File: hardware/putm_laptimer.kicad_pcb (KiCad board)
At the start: 4 copper layers, 83 x 63.5 mm, 54 parts, among them J1 Conn_01x22, J2 Conn_01x22, J3 Conn_01x22, J4 Conn_01x22, J5 2092-1372, J6 2092-1372, J7 Conn_02x05_Odd_Even, J8 Conn_01x09, SW1 SW_Push, SW2 SW_Push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

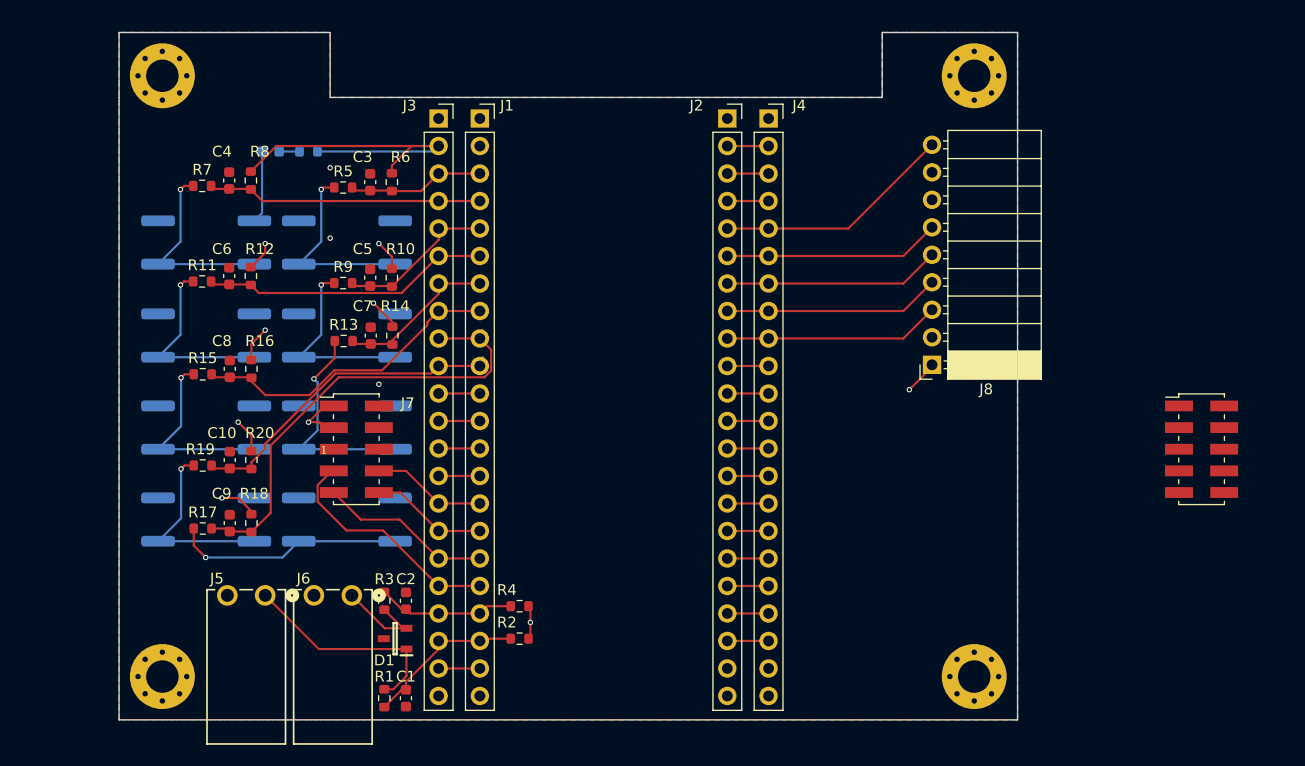
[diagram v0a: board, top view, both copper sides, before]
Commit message: deleted buttons on board and added hawrin connector
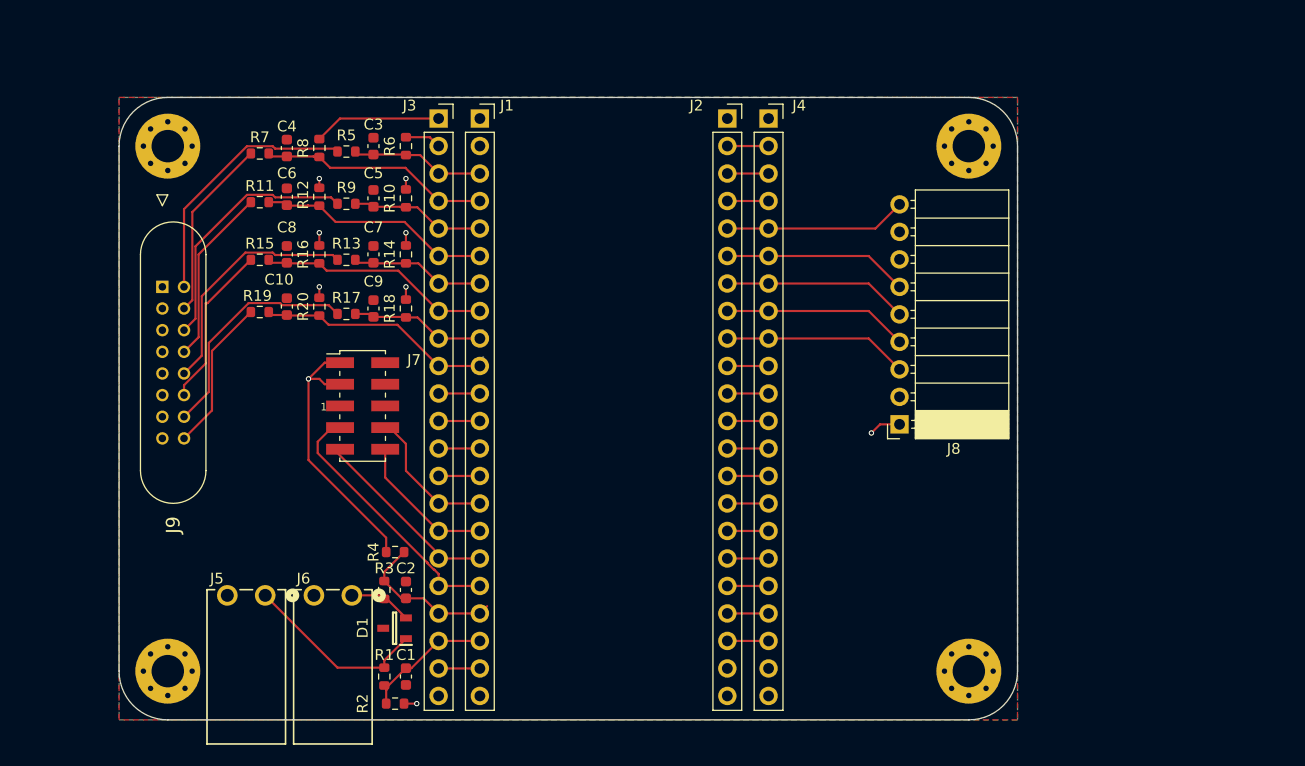
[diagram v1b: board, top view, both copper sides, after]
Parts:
- removed D2: Red, LED_SMD:LED_0603_1608Metric
- removed the J7 at (216.0, 91.5)
- removed R21: 330R, Resistor_SMD:R_0603_1608Metric
- removed SW1, SW2, SW3, SW4, SW5, SW6, SW7, SW8: SW_Push, Button_Switch_SMD:SW_Push_1P1T_NO_CK_KSC6xxG
- added J9: M80-5001605, Footprint:M80-50016YY_2, F.Cu at (120.0, 76.5)
- J5, J6: value 2092-1372 -> 2091-1372
- moved R18 24.4 mm to (142.5, 78.5)
- moved C9 23.9 mm to (139.5, 78.5)
- moved R17 23.9 mm to (137.0, 79.0)
- moved R20 15.5 mm to (134.5, 78.3)
- moved C10 15.1 mm to (131.5, 78.3)
- moved R19 15.1 mm to (129.0, 78.8)
- moved R2 13.0 mm to (141.5, 115.0)
- moved R4 12.5 mm to (141.5, 101.0), turned to 180 degrees
- moved R16 12.3 mm to (134.5, 73.5)
- moved C8 11.8 mm to (131.5, 73.5)
- moved R15 11.8 mm to (129.0, 74.0)
- moved R12 9.68 mm to (134.5, 68.2)
- moved C6 9.06 mm to (131.5, 68.2)
- moved R11 9.06 mm to (129.0, 68.7)
- moved R14 7.60 mm to (142.5, 73.5)
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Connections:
- net /IO15_DRIVER_BTN renamed /IO15_PIN
- net /IO16_ADD1_BTN renamed /IO16_PIN
- net /IO17_ADD2_BTN renamed /IO17_PIN
- net /IO4_STOP_BTN renamed /IO4_PIN
- net /IO5_WIFI_BTN renamed /IO5_PIN
- net /IO6_DOO_BTN renamed /IO6_PIN
- net /IO7_OC_BTN renamed /IO7_PIN
- C3 pad 1: /RST_BTN -> /RST_PIN
- J1 pad 3: /RST_BTN -> /RST_PIN
- J3 pad 3: /RST_BTN -> /RST_PIN
- R11 pad 2: Net-(R11-Pad2) -> /DOO_BTN
- R13 pad 2: Net-(R13-Pad2) -> /OC_BTN
- R15 pad 2: Net-(R15-Pad2) -> /DRIVER_BTN
- R17 pad 2: Net-(R17-Pad2) -> /ADD1_BTN
- R19 pad 2: Net-(R19-Pad2) -> /ADD2_BTN
- R5 pad 1: /RST_BTN -> /RST_PIN
- R5 pad 2: Net-(R5-Pad2) -> /RST_BTN
- R6 pad 1: /RST_BTN -> /RST_PIN
- R7 pad 2: Net-(R7-Pad2) -> /STOP_BTN
- R9 pad 2: Net-(R9-Pad2) -> /WIFI_BTN
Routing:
- net /IO16_PIN: track 43.4 -> 12.8 mm
- net /WIFI_BTN: track 0.00 -> 23.6 mm
- net /OC_BTN: track 0.00 -> 22.3 mm
- net /ADD1_BTN: track 0.00 -> 21.6 mm
- net Net-(R17-Pad2): track 21.3 -> 0.00 mm, vias 1 -> 0
- net Net-(R13-Pad2): track 20.6 -> 0.00 mm, vias 1 -> 0
- net Net-(R7-Pad2): track 18.0 -> 0.00 mm, vias 1 -> 0
- net Net-(R5-Pad2): track 17.9 -> 0.00 mm, vias 1 -> 0
- net Net-(R19-Pad2): track 17.8 -> 0.00 mm, vias 1 -> 0
- net Net-(R11-Pad2): track 17.7 -> 0.00 mm, vias 1 -> 0
- net Net-(R9-Pad2): track 17.7 -> 0.00 mm, vias 1 -> 0
- net Net-(R15-Pad2): track 17.7 -> 0.00 mm, vias 1 -> 0
- net /STOP_BTN: track 0.00 -> 16.9 mm
- net /DOO_BTN: track 0.00 -> 16.4 mm
- net /DRIVER_BTN: track 0.00 -> 15.2 mm
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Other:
- board size 83 x 63.5 mm -> 83 x 57.5 mm

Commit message: placed rtc connectors on pcb
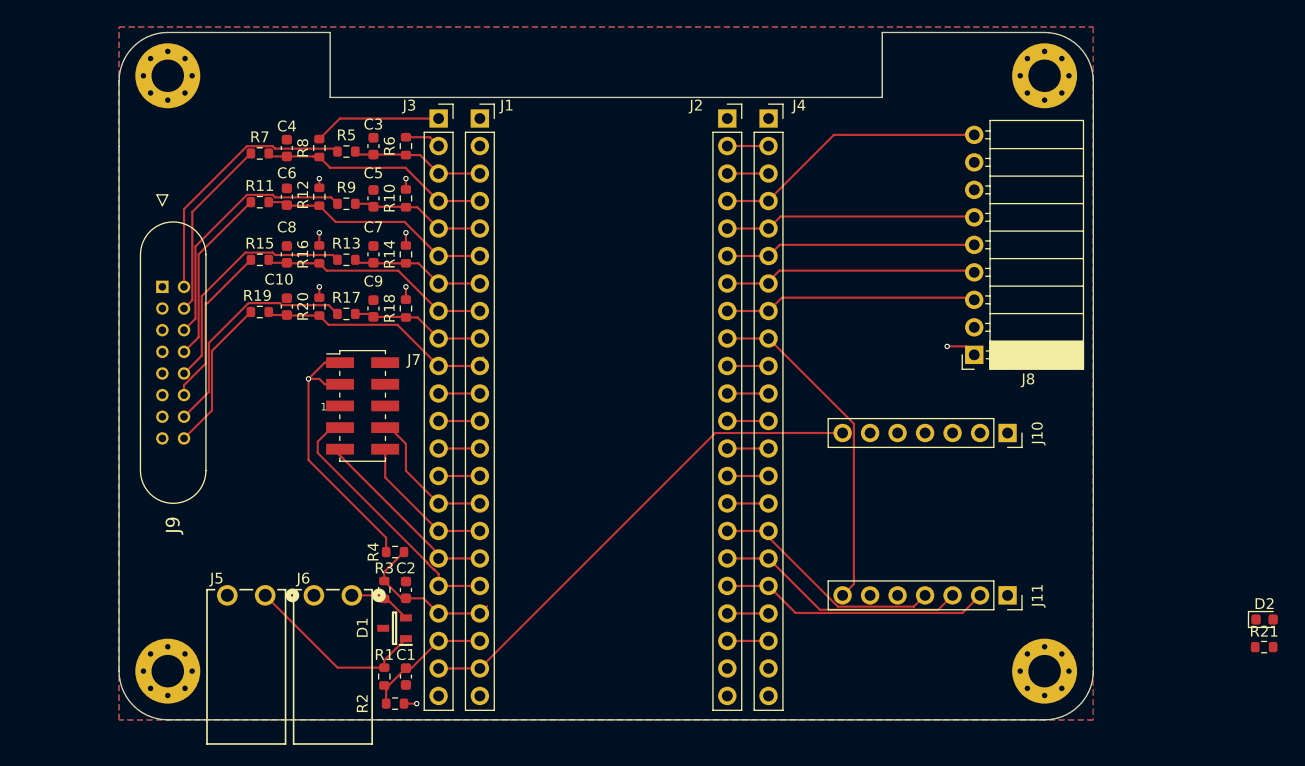
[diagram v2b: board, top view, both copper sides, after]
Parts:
- added D2: Red, LED_SMD:LED_0603_1608Metric, F.Cu at (221.8, 107.2)
- added J10: Conn_01x07, Connector_PinSocket_2.54mm:PinSocket_1x07_P2.54mm_Vertical, F.Cu at (198.1, 90.0)
- added J11: Conn_01x07, Connector_PinSocket_2.54mm:PinSocket_1x07_P2.54mm_Vertical, F.Cu at (198.1, 105.0)
- added R21: 330R, Resistor_SMD:R_0603_1608Metric, F.Cu at (221.8, 109.8)
- moved REF** 9.55 mm to (201.5, 57.0)
- moved J8 9.42 mm to (195.0, 82.8)
- moved REF** 7.00 mm to (201.5, 112.0)
- moved REF** 6.50 mm to (120.5, 57.0)
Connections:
- net /IO21_PIN renamed /IO21_RTC_I2C_SCL
- net /IO47_PIN renamed /IO47_RTC_I2C_SDA
- net /IO48_PIN renamed /IO48_RTC_CLKOUT
- C1 pad 1: /IO14_GATE1_PIN -> /IO14_GATE1
- C2 pad 1: /IO13_GATE2_PIN -> /IO13_GATE2
- J1 pad 19: /IO13_GATE2_PIN -> /IO13_GATE2
- J1 pad 20: /IO14_GATE1_PIN -> /IO14_GATE1
- J2 pad 4: /IO1_PIN -> /IO1_SD_CD
- J2 pad 5: /IO2_SD_CD -> /IO2_SD_SPI_CS
- J2 pad 6: /IO42_SD_SPI_CS -> /IO42_SD_SPI_CLK
- J2 pad 7: /IO41_SD_SPI_CLK -> /IO41_SD_SPI_MOSI
- J2 pad 8: /IO40_SD_SPI_MOSI -> /IO40_SD_SPI_MISO
- J2 pad 9: /IO39_SD_SPI_MISO -> /IO39_RTC_NINT
- J4 pad 4: /IO1_PIN -> /IO1_SD_CD
- J4 pad 5: /IO2_SD_CD -> /IO2_SD_SPI_CS
- J4 pad 6: /IO42_SD_SPI_CS -> /IO42_SD_SPI_CLK
- J4 pad 7: /IO41_SD_SPI_CLK -> /IO41_SD_SPI_MOSI
- J4 pad 8: /IO40_SD_SPI_MOSI -> /IO40_SD_SPI_MISO
- J4 pad 9: /IO39_SD_SPI_MISO -> /IO39_RTC_NINT
- J8 pad 3: /IO39_SD_SPI_MISO -> /IO40_SD_SPI_MISO
- J8 pad 4: /IO40_SD_SPI_MOSI -> /IO41_SD_SPI_MOSI
- J8 pad 5: /IO41_SD_SPI_CLK -> /IO42_SD_SPI_CLK
- J8 pad 6: /IO42_SD_SPI_CS -> /IO2_SD_SPI_CS
- J8 pad 9: /IO2_SD_CD -> /IO1_SD_CD
- R1 pad 1: /IO14_GATE1_PIN -> /IO14_GATE1
- R2 pad 1: /IO14_GATE1_PIN -> /IO14_GATE1
- R3 pad 1: /IO13_GATE2_PIN -> /IO13_GATE2
- R4 pad 1: /IO13_GATE2_PIN -> /IO13_GATE2
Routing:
- net +5V: track 3.81 -> 46.3 mm
- net /IO39_RTC_NINT: track 0.00 -> 31.2 mm
- net /IO1_SD_CD: track 0.00 -> 25.4 mm
- net /IO41_SD_SPI_MOSI: track 0.00 -> 23.5 mm
- net /IO40_SD_SPI_MISO: track 0.00 -> 23.4 mm
- net /IO2_SD_SPI_CS: track 0.00 -> 23.3 mm
- net /IO42_SD_SPI_CLK: track 0.00 -> 23.2 mm
- net /IO21_RTC_I2C_SCL: track 3.81 -> 25.1 mm
- net /IO47_RTC_I2C_SDA: track 3.81 -> 23.3 mm
- net /IO48_RTC_CLKOUT: track 3.81 -> 21.9 mm
- net /IO41_SD_SPI_CLK: track 17.1 -> 0.00 mm
- net /IO39_SD_SPI_MISO: track 17.1 -> 0.00 mm
- net /IO42_SD_SPI_CS: track 17.1 -> 0.00 mm
- net /IO40_SD_SPI_MOSI: track 17.1 -> 0.00 mm
- net /IO2_SD_CD: track 16.8 -> 0.00 mm
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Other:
- board size 83 x 57.5 mm -> 90 x 63.5 mm

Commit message: changed harwin connector to connect power led, updated cleareance and net width
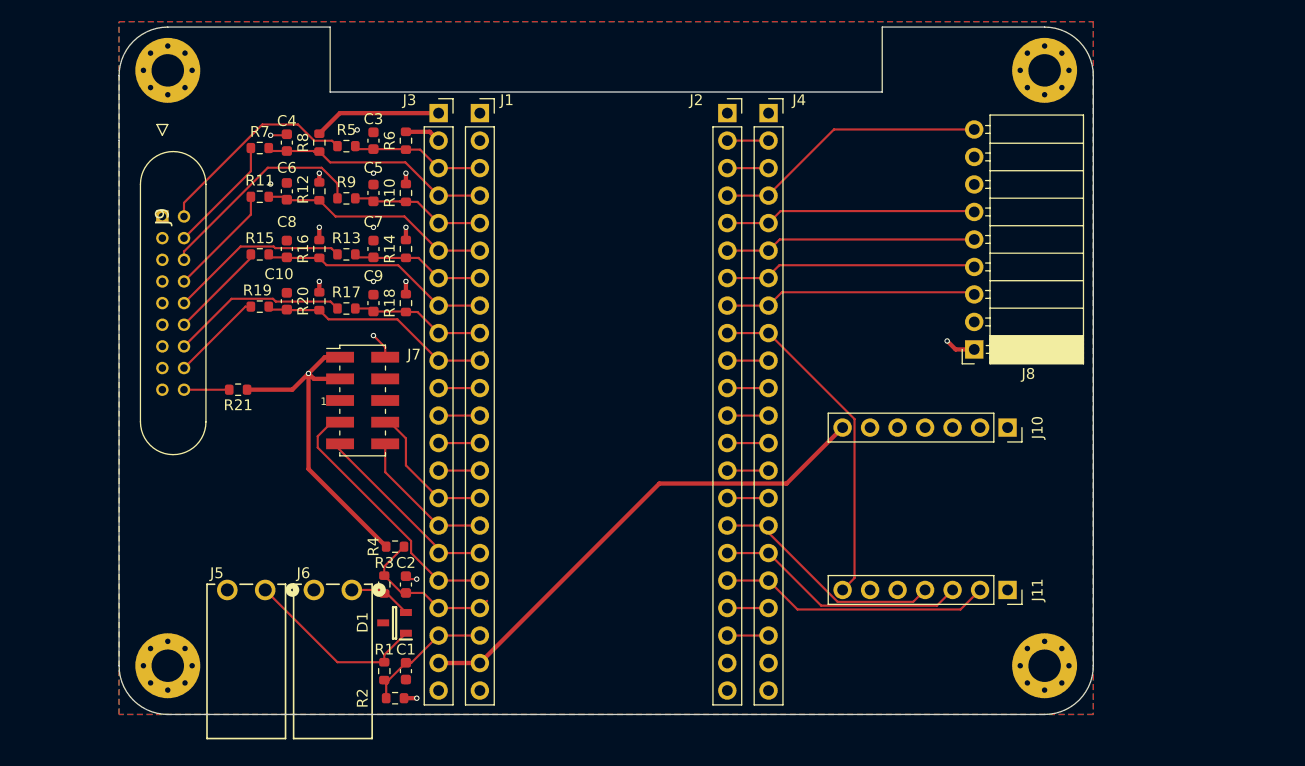
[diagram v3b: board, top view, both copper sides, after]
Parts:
- removed D2: Red, LED_SMD:LED_0603_1608Metric
- J9: value M80-5001605 -> M80-5001805; footprint Footprint:M80-50016YY_2 -> Footprint:M80-50018YY_2
- moved R21 97.7 mm to (127.0, 86.0), turned to 180 degrees
- moved J9 6.50 mm to (120.0, 70.0)
- moved C1 0.50 mm to (142.5, 112.0)
- moved C10 0.50 mm to (131.5, 77.8)
- moved C2 0.50 mm to (142.5, 104.0)
- moved C3 0.50 mm to (139.5, 63.0)
- moved C4 0.50 mm to (131.5, 63.2)
- moved C5 0.50 mm to (139.5, 67.8)
- moved C6 0.50 mm to (131.5, 67.7)
- moved C7 0.50 mm to (139.5, 73.0)
- moved C8 0.50 mm to (131.5, 73.0)
- moved C9 0.50 mm to (139.5, 78.0)
- moved D1 0.50 mm to (141.4, 107.5)
- moved J1 0.50 mm to (149.3, 60.5)
- moved J10 0.50 mm to (198.1, 89.5)
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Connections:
- J3 pad 19: /IO13_GATE2_PIN -> /IO13_GATE2
- J3 pad 20: /IO14_GATE1_PIN -> /IO14_GATE1
- J9 pad 10: /STOP_BTN -> /RST_BTN
- J9 pad 11: /WIFI_BTN -> /STOP_BTN
- J9 pad 12: /DOO_BTN -> /WIFI_BTN
- J9 pad 13: /OC_BTN -> /DOO_BTN
- J9 pad 14: /DRIVER_BTN -> /OC_BTN
- J9 pad 15: /ADD1_BTN -> /DRIVER_BTN
- J9 pad 16: /ADD2_BTN -> /ADD1_BTN
- J9 pad 9: /RST_BTN -> GND
- R21 pad 2: Net-(D2-A) -> /PWR_LED
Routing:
- net /IO13_GATE2_PIN: track 14.6 -> 0.00 mm
- net /IO13_GATE2: track 0.00 -> 14.6 mm
- net /IO14_GATE1_PIN: track 13.5 -> 0.00 mm
- net /IO14_GATE1: track 0.00 -> 13.5 mm
- net +3V3: track 50.9 -> 58.4 mm
- net /DRIVER_BTN: track 15.2 -> 9.06 mm
- net /DOO_BTN: track 16.4 -> 10.4 mm
- net /STOP_BTN: track 16.9 -> 10.9 mm
- net /ADD2_BTN: track 14.2 -> 8.53 mm
- net /OC_BTN: track 22.3 -> 16.6 mm
- net /ADD1_BTN: track 21.6 -> 16.4 mm
- net GND: track 0.00 -> 5.10 mm, vias 0 -> 8
- net /RST_BTN: track 24.0 -> 19.3 mm
- net /PWR_LED: track 0.00 -> 4.17 mm
- net /WIFI_BTN: track 23.6 -> 20.1 mm

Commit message: changed element placement
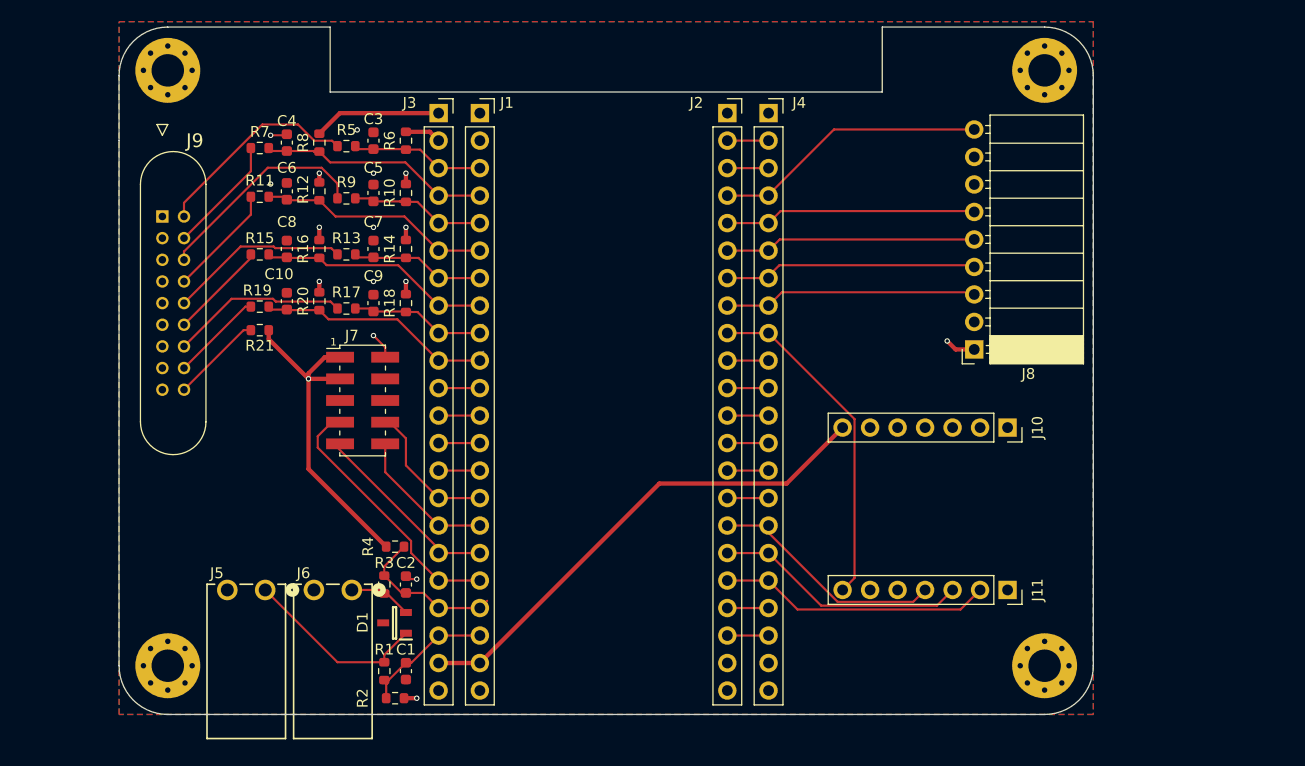
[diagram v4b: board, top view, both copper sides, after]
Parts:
- moved R21 5.85 mm to (129.0, 80.5)
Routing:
- net /PWR_LED: track 4.17 -> 8.45 mm
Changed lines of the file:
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@@
 		(tags "Through hole socket strip THT 1x22 2.54mm single row")
 		(property "Reference" "J1"
-			(at 2.5 -1.2 0)
+			(at 2.5 -0.95 0)
 			(layer "F.SilkS")
 			(effects
@@
 	(footprint "Resistor_SMD:R_0603_1608Metric"
 		(layer "F.Cu")
-		(at 127 86 180)
+		(at 129 80.5 180)
 		(descr "Resistor SMD 0603 (1608 Metric), square (rectangular) end terminal, IPC-7351 nominal, (Body size source: IPC-SM-782 page 72, https://www.pcb-3d.com/wordpress/wp-content/uploads/ipc-sm-782a_amendment_1_and_2.pdf), generated with kicad-footprint-generator")
 		(tags "resistor")
@@
 		(tags "Through hole socket strip THT 1x22 2.54mm single row")
 		(property "Reference" "J4"
-			(at 2.83 -1.2 0)
+			(at 2.83 -0.95 0)
 			(layer "F.SilkS")
 			(effects
@@
 		(tags "Through hole socket strip THT 1x22 2.54mm single row")
 		(property "Reference" "J3"
-			(at -2.69 -1.2 0)
+			(at -2.69 -0.95 0)
 			(layer "F.SilkS")
 			(effects
@@
 		(tags "Through hole socket strip THT 1x22 2.54mm single row")
 		(property "Reference" "J2"
-			(at -2.86 -1.2 0)
+			(at -2.86 -0.95 0)
 			(layer "F.SilkS")
 			(effects
@@
 		(tags "Connector")
 		(property "Reference" "J9"
-			(at 0 0 90)
+			(at -7 -3 180)
 			(layer "F.SilkS")
 			(effects
@@
 		(tags "Surface mounted pin header SMD 2x05 2.00mm double row")
 		(property "Reference" "J7"
-			(at 4.75 -4.25 0)
+			(at -1 -6 0)
 			(layer "F.SilkS")
 			(effects
@@
 		(tags "resistor")
 		(property "Reference" "R4"
-			(at 2 0 90)
+			(at 2.5 0 90)
 			(layer "F.SilkS")
 			(effects
@@
 	)
 	(gr_text "1"
-		(at 134.6 87.5 0)
+		(at 135.5 82 0)
 		(layer "F.SilkS")
 		(effects
@@
 	)
 	(segment
-		(start 133.5 93.325)
-		(end 140.675 100.5)
+		(start 133.5 84.5)
+		(end 135 83)
 		(width 0.4)
 		(layer "F.Cu")
@@
 	)
 	(segment
-		(start 127.825 86)
-		(end 132 86)
+		(start 193.28 82.28)
+		(end 192.5 81.5)
 		(width 0.4)
 		(layer "F.Cu")
@@
 	)
 	(segment
-		(start 193.28 82.28)
-		(end 192.5 81.5)
+		(start 142.5 77.175)
+		(end 142.5 76)
 		(width 0.4)
 		(layer "F.Cu")
@@
 	)
 	(segment
-		(start 136.415 85)
-		(end 134 85)
+		(start 133.5 85)
+		(end 133.5 93.325)
 		(width 0.4)
 		(layer "F.Cu")
@@
 	)
 	(segment
-		(start 142.5 77.175)
-		(end 142.5 76)
+		(start 133.5 93.325)
+		(end 140.675 100.5)
 		(width 0.4)
 		(layer "F.Cu")
@@
 	)
 	(segment
-		(start 132 86)
+		(start 133.5 85)
 		(end 133.5 84.5)
 		(width 0.4)
@@
 	)
 	(segment
-		(start 133.5 84.5)
-		(end 133.5 93.325)
-		(width 0.4)
-		(layer "F.Cu")
-		(net 13)
-	)
-	(segment
 		(start 195 82.28)
 		(end 193.28 82.28)
@@
 	)
 	(segment
-		(start 136.415 83)
-		(end 135 83)
+		(start 129.825 81.325)
+		(end 133.5 85)
 		(width 0.4)
 		(layer "F.Cu")
@@
 	)
 	(segment
-		(start 135 83)
-		(end 133.5 84.5)
+		(start 133.5 85)
+		(end 136.415 85)
 		(width 0.4)
 		(layer "F.Cu")
@@
 	)
 	(segment
-		(start 134 85)
-		(end 133.5 84.5)
+		(start 143.5 114.5)
+		(end 142.325 114.5)
 		(width 0.4)
 		(layer "F.Cu")
@@
 	)
 	(segment
-		(start 143.5 114.5)
-		(end 142.325 114.5)
+		(start 135 83)
+		(end 136.415 83)
 		(width 0.4)
 		(layer "F.Cu")
@@
 	)
 	(segment
+		(start 129.825 80.5)
+		(end 129.825 81.325)
+		(width 0.4)
+		(layer "F.Cu")
+		(net 13)
+	)
+	(segment
 		(start 142.5 72.175)
 		(end 142.5 71)
@@
 	)
 	(via
-		(at 133.5 84.5)
+		(at 133.5 85)
 		(size 0.5)
 		(drill 0.3)
@@
 	)
 	(segment
-		(start 126.175 86)
-		(end 122 86)
+		(start 122 86)
+		(end 127.5 80.5)
+		(width 0.2)
+		(layer "F.Cu")
+		(net 64)
+	)
+	(segment
+		(start 127.5 80.5)
+		(end 128.175 80.5)
 		(width 0.2)
 		(layer "F.Cu")
